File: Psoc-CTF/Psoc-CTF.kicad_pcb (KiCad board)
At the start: 2 copper layers, 68.6 x 53.3 mm, 62 parts, among them IC1 CY8C4248LQI-BL583, J3 PROG, P1 Power, P2 Analog, P3 Digital, P4 Digital, P5 CONN_01X01, P6 CONN_01X01, P7 CONN_01X01, P8 CONN_01X01, U1 AMS1117-3.3, U2 AMS1117-5.0, U3 ESP32-WROOM-32D, U4 23LC1024-E_SN, U5 SST25VF512-20-4C-SAE

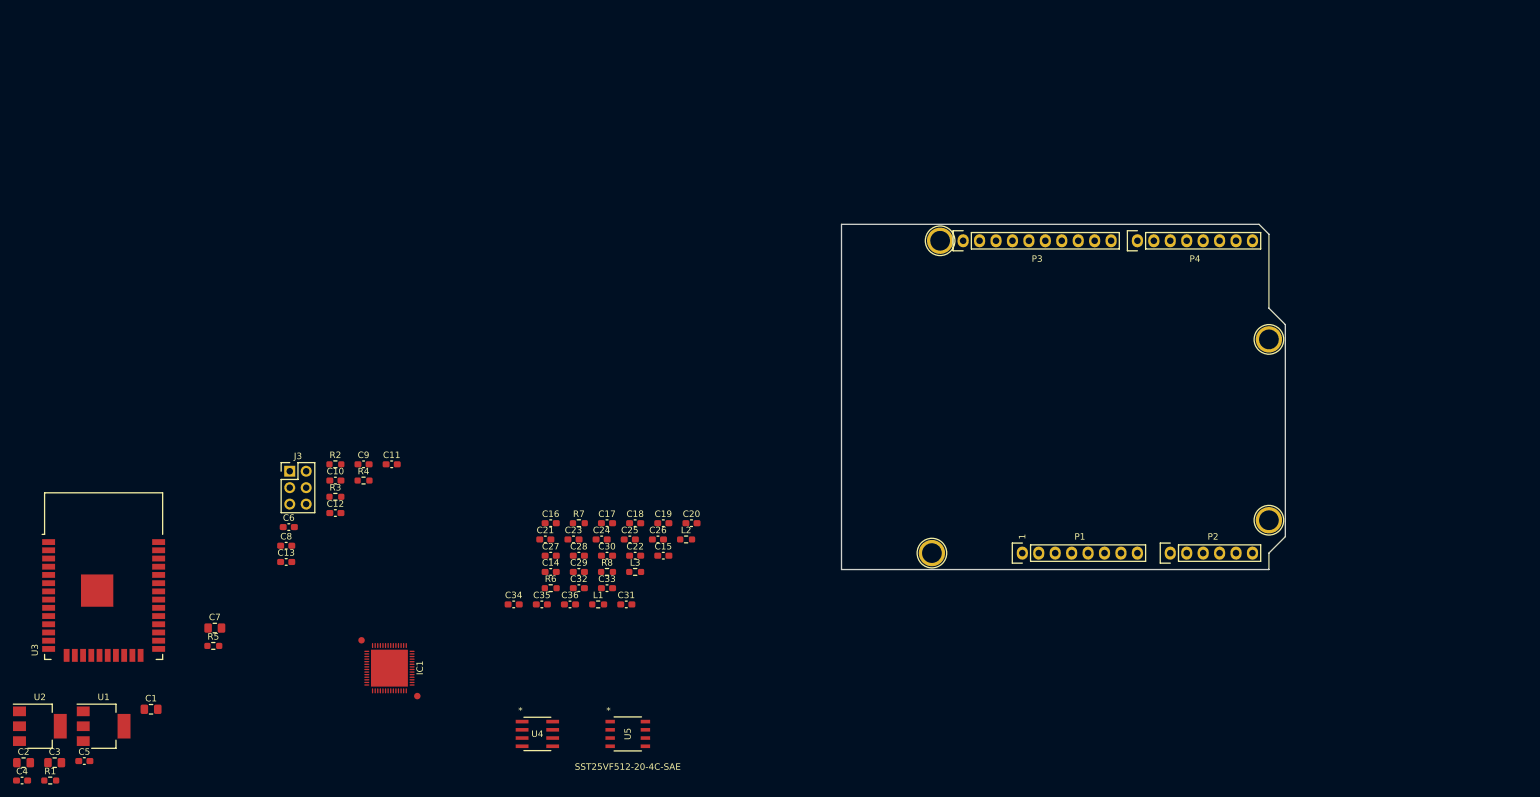
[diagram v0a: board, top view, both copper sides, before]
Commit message: Se retira las memorias flash y Ram por spi y se coloca una F-RAM por i2c
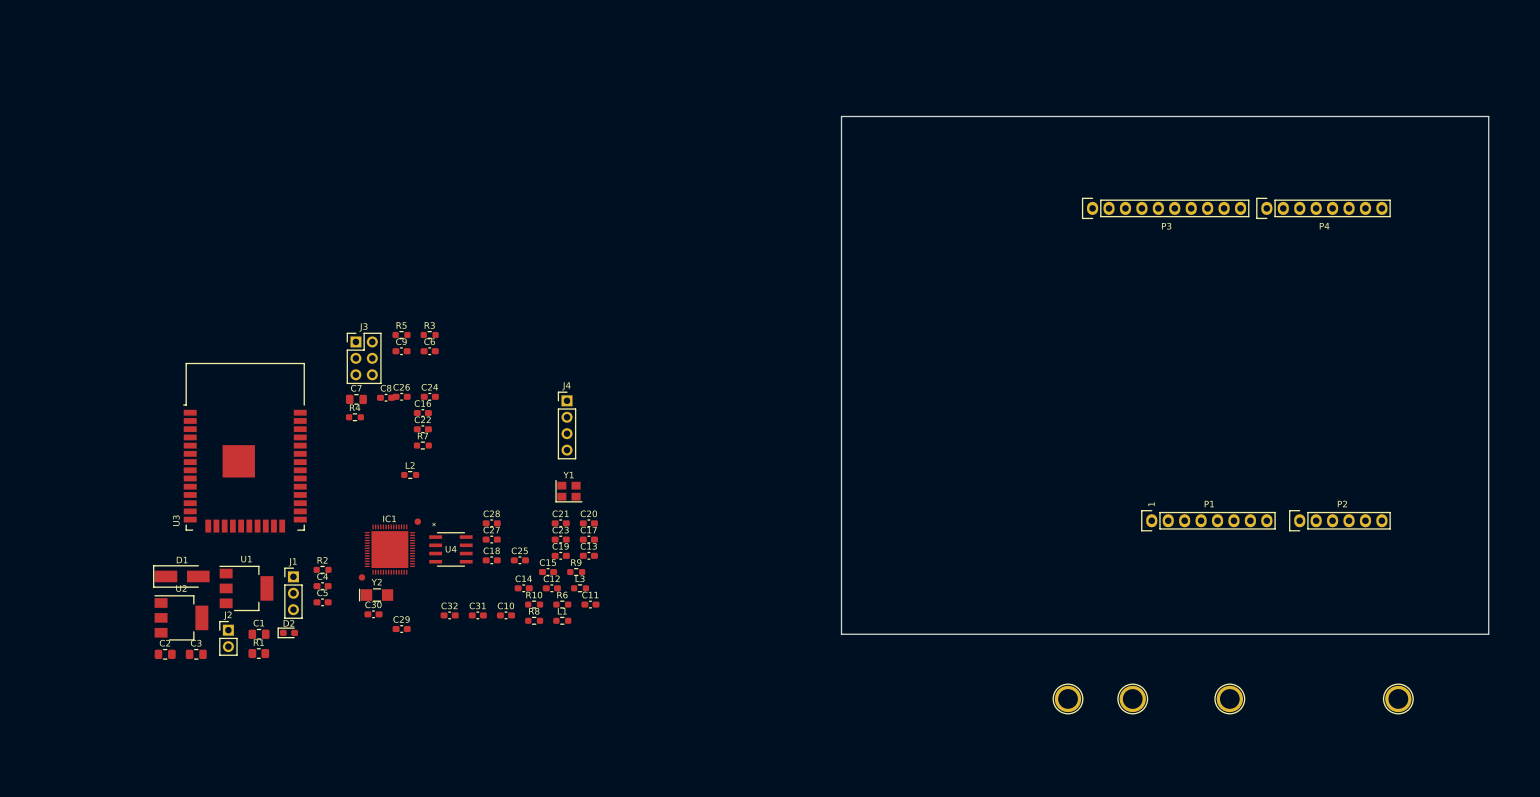
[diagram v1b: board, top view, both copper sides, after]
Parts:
- removed C33, C34: 1uF, Capacitor_SMD:C_0603_1608Metric_Pad1.08x0.95mm_HandSolder
- removed C35, C36: 0.1uF, Capacitor_SMD:C_0603_1608Metric_Pad1.08x0.95mm_HandSolder
- removed U5: SST25VF512-20-4C-SAE, Psoc-CTF:SST25VF512-20-4C-SAE
- added D1: EGF1D, Diode_SMD:D_SMA_Handsoldering, F.Cu at (9.12, 127.4)
- added D2: LED, LED_SMD:LED_0603_1608Metric_Pad1.05x0.95mm_HandSolder, F.Cu at (25.6, 136.2)
- added J1: Conn_01x03, Connector_PinHeader_2.54mm:PinHeader_1x03_P2.54mm_Vertical, F.Cu at (26.3, 127.5)
- added J2: Conn_01x02, Connector_PinHeader_2.54mm:PinHeader_1x02_P2.54mm_Vertical, F.Cu at (16.3, 135.7)
- added J4: Conn_01x04, Connector_PinHeader_2.54mm:PinHeader_1x04_P2.54mm_Vertical, F.Cu at (68.6, 100.3)
- added R10: 0, Resistor_SMD:R_0603_1608Metric_Pad0.98x0.95mm_HandSolder, F.Cu at (63.5, 131.8)
- added R9: 0, Resistor_SMD:R_0603_1608Metric_Pad0.98x0.95mm_HandSolder, F.Cu at (70.0, 126.8)
- added Y1: 24MHz, Crystal:Crystal_SMD_3225-4Pin_3.2x2.5mm, F.Cu at (68.9, 114.3)
- added Y2: 32.768Khz, Crystal:Crystal_SMD_EuroQuartz_EQ161-2Pin_3.2x1.5mm_HandSoldering, F.Cu at (39.2, 130.3)
- C10: value 1uF -> 36pF
- C11: value 1uF -> 18pF
- C13, C16, C22: value 0.1uF -> 1uF
- C14: value 36pF -> 1uF
- C15: value 18pF -> 2200pF
- C17, C18, C23, C24: value 1uF -> 0.1uF
- C19: value 2200pF -> 1uF
- C21: value 0.1uF -> 10000pF
- C25: value 10000pF -> 1uF
- R1: value 1K -> 0; footprint Resistor_SMD:R_0603_1608Metric_Pad0.98x0.95mm_HandSolder -> Resistor_SMD:R_0805_2012Metric_Pad1.20x1.40mm_HandSolder
- R2: value 10K -> 1K
- R3, R7: value 0 -> 10K
- U4: value 23LC1024-E_SN -> FM24C04B-GTR
- moved P7 76.8 mm to (156.0, 146.4)
- moved R5 56.2 mm to (43.0, 90.1)
- moved P8 55.9 mm to (171.0, 146.4)
- moved C4 55.3 mm to (30.8, 128.9)
- moved C13 46.8 mm to (72.0, 124.2)
- moved C26 45.3 mm to (43.0, 99.7)
- moved C5 44.2 mm to (30.8, 131.4)
- moved L2 43.8 mm to (44.4, 111.8)
- moved C7 41.6 mm to (36.0, 100.1)
- moved C22 38.2 mm to (46.3, 104.7)
- moved R1 37.7 mm to (21.0, 139.3)
- moved C11 37.6 mm to (72.2, 131.8)
- moved C30 37.2 mm to (38.7, 133.3)
- moved C12 35.4 mm to (66.2, 129.3)
- moved C6 34.8 mm to (47.4, 92.6)
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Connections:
- net Net-(IC1-Pad19) renamed /MCU_Target/11(**/MOSI)
- net Net-(IC1-Pad20) renamed /MCU_Target/12(MISO)
- net Net-(IC1-Pad21) renamed /MCU_Target/10(**/SS)
- net Net-(IC1-Pad22) renamed /MCU_Target/13(SCK)
- net Net-(IC1-Pad24) renamed /MCU_Target/9(**)
- net Net-(IC1-Pad25) renamed /MCU_Target/8
- net Net-(IC1-Pad28) renamed /MCU_Target/7
- net Net-(IC1-Pad29) renamed /MCU_Target/6(**)
- net Net-(IC1-Pad30) renamed /MCU_Target/5(**)
- net Net-(IC1-Pad31) renamed /MCU_Target/4
- net Net-(IC1-Pad34) renamed /MCU_Target/2
- net Net-(IC1-Pad35) renamed /MCU_Target/3(**)
- net Net-(IC1-Pad47) renamed /MCU_Target/A0
- net Net-(IC1-Pad48) renamed /MCU_Target/A1
- net Net-(IC1-Pad49) renamed /MCU_Target/A2
- net Net-(IC1-Pad50) renamed /MCU_Target/A3
- C10 pad 1: VDD -> /MCU_Target/XTAL32I
- C11 pad 1: VDD -> /MCU_Target/XTAL32O
- C12 pad 1: VDD -> /MCU_Target/XRES
- C13 pad 1: VDD -> /MCU_Target/VDDD
- C14 pad 1: /MCU_Target/XTAL32I -> /MCU_Target/VDDR
- C15 pad 1: /MCU_Target/XTAL32O -> /MCU_Target/P4.0
- C16 pad 1: /MCU_Target/XRES -> /MCU_Target/VCCD
- C19 pad 1: /MCU_Target/P4.0 -> /MCU_Target/VDDD
- C20 pad 1: /MCU_Target/VCCD -> /MCU_Target/VDDR
- C21 pad 1: /MCU_Target/VDDD -> /MCU_Target/P4.1
- C22 pad 1: /MCU_Target/VDDR -> /MCU_Target/VREF
- C25 pad 1: /MCU_Target/P4.1 -> /MCU_Target/VDDA
- C26 pad 1: /MCU_Target/VREF -> /MCU_Target/VDDR
- C27 pad 1: /MCU_Target/VDDD -> /MCU_Target/VDDA
- C31 pad 1: /MCU_Target/VDDA -> /MCU_Target/VDDR
- C32 pad 1: /MCU_Target/VDDR -> /MCU_Target/VDDA
- IC1 pad 51: Net-(IC1-Pad51) -> /MCU_Target/T_MCU_SDA
- IC1 pad 52: Net-(IC1-Pad52) -> /MCU_Target/T_MCU_SCL
- R1 pad 2: Net-(D2-Pad2) -> +3V3
- R2 pad 2: /MONITOR/EN -> Net-(D2-Pad2)
- R3 pad 1: Net-(R3-Pad1) -> VDD
- R3 pad 2: GND -> /MONITOR/EN
- R4 pad 2: Net-(R4-Pad2) -> /MCU_Target/T_MCU_SDA
- R5 pad 1: VDD -> /MCU_Target/T_MCU_SCL
- R5 pad 2: Net-(R5-Pad2) -> VDD
- R7 pad 1: /MCU_Target/P4.0 -> Net-(R7-Pad1)
- R8 pad 1: /MCU_Target/VCCD -> VDD
- R8 pad 2: /MCU_Target/VDDD -> Net-(R7-Pad1)
- U3 pad 30: /MONITOR/SPI_CLK -> Net-(U3-Pad30)
- U3 pad 31: /MONITOR/SPI_MISO -> Net-(U3-Pad31)
- U3 pad 33: /MONITOR/CE_FLASH -> /MCU_Target/T_MCU_SDA
- U3 pad 36: /MONITOR/CE_RAM -> /MCU_Target/T_MCU_SCL
- U3 pad 37: /MONITOR/SPI_MOSI -> Net-(U3-Pad37)
- U4 pad 1: /MONITOR/CE_RAM -> Net-(U4-Pad1)
- U4 pad 2: /MONITOR/SPI_MISO -> GND
- U4 pad 3: Net-(U4-Pad3) -> GND
- U4 pad 5: /MONITOR/SPI_MOSI -> /MCU_Target/T_MCU_SDA
- U4 pad 6: /MONITOR/SPI_CLK -> /MCU_Target/T_MCU_SCL
- U4 pad 7: Net-(R5-Pad2) -> Net-(R7-Pad1)
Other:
- board size 68.6 x 53.3 mm -> 100 x 80 mm

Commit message: Antena agregada, pines de programación SWD
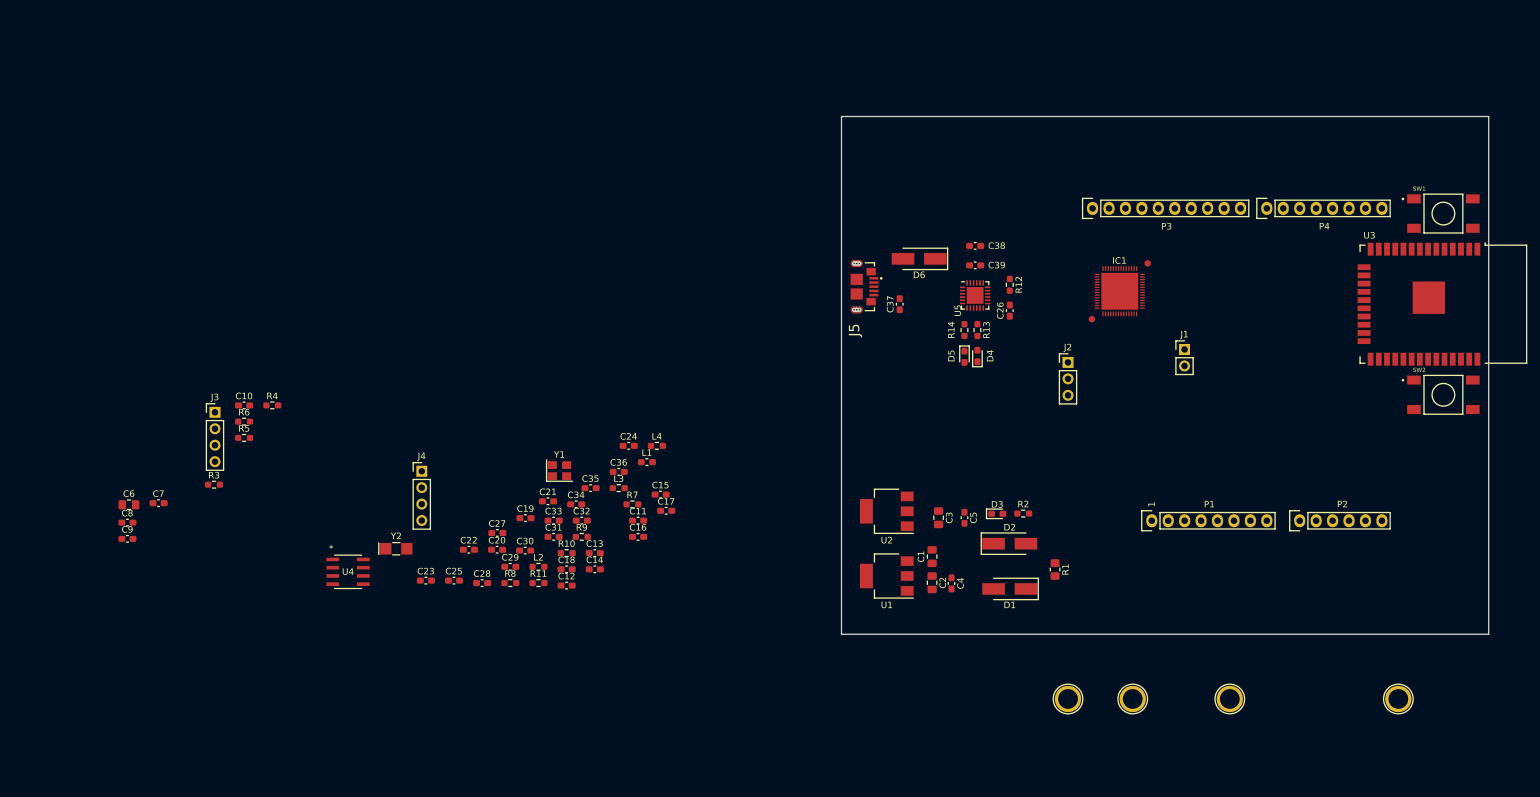
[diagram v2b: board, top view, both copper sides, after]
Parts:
- added C33: 1uF, Capacitor_SMD:C_0603_1608Metric_Pad1.08x0.95mm_HandSolder, F.Cu at (66.5, 118.8)
- added C34: 1uF, Capacitor_SMD:C_0603_1608Metric_Pad1.08x0.95mm_HandSolder, F.Cu at (70.0, 116.3)
- added C35: 0.1uF, Capacitor_SMD:C_0603_1608Metric_Pad1.08x0.95mm_HandSolder, F.Cu at (72.2, 113.8)
- added C36: 0.1uF, Capacitor_SMD:C_0603_1608Metric_Pad1.08x0.95mm_HandSolder, F.Cu at (76.6, 111.3)
- added C37: 0.1uF, Capacitor_SMD:C_0603_1608Metric_Pad1.08x0.95mm_HandSolder, F.Cu at (120.0, 85.4)
- added C38: 1uF, Capacitor_SMD:C_0603_1608Metric_Pad1.08x0.95mm_HandSolder, F.Cu at (131.6, 76.4)
- added C39: 0.1uF, Capacitor_SMD:C_0603_1608Metric_Pad1.08x0.95mm_HandSolder, F.Cu at (131.6, 79.4)
- added D3: LED, LED_SMD:LED_0603_1608Metric_Pad1.05x0.95mm_HandSolder, F.Cu at (135.1, 117.8)
- added D4: LED, LED_SMD:LED_0603_1608Metric_Pad1.05x0.95mm_HandSolder, F.Cu at (132.0, 93.4)
- added D5: LED, LED_SMD:LED_0603_1608Metric_Pad1.05x0.95mm_HandSolder, F.Cu at (130.0, 93.5)
- added D6: SSA14, Diode_SMD:D_SMA_Handsoldering, F.Cu at (123.0, 78.4)
- added J5: USB3076-XX-X_REVC, Psoc-CTF:microUSB, F.Cu at (113.3, 82.7)
- added L4: FBMH1608HM331-T, Resistor_SMD:R_0603_1608Metric_Pad0.98x0.95mm_HandSolder, F.Cu at (82.5, 107.3)
- added R11: 0, Resistor_SMD:R_0603_1608Metric_Pad0.98x0.95mm_HandSolder, F.Cu at (64.2, 128.5)
- added R12: 10k, Resistor_SMD:R_0603_1608Metric_Pad0.98x0.95mm_HandSolder, F.Cu at (137.0, 82.4)
- added R13: 1K, Resistor_SMD:R_0603_1608Metric_Pad0.98x0.95mm_HandSolder, F.Cu at (132.0, 89.4)
- added R14: 1K, Resistor_SMD:R_0603_1608Metric_Pad0.98x0.95mm_HandSolder, F.Cu at (130.0, 89.4)
- added SW1: FSM4JSMATR, Psoc-CTF:Push_button_FSM4JSMATR, F.Cu at (204.0, 71.4)
- added SW2: FSM4JSMATR, Psoc-CTF:Push_button_FSM4JSMATR, F.Cu at (204.0, 99.4)
- added U5: CY7C65211-24LTXI, Package_DFN_QFN:QFN-24-1EP_4x4mm_P0.5mm_EP2.6x2.6mm, F.Cu at (131.6, 84.0)
- C10: value 36pF -> 0.1uF
- C11: value 18pF -> 36pF
- C12: value 0.1uF -> 18pF
- C13, C19, C25, C30, C8: value 1uF -> 0.1uF
- C15: value 2200pF -> 1uF
- C16: value 1uF -> 2200pF
- C17, C23, C27, C28: value 0.1uF -> 1uF
- C21: value 10000pF -> 1uF
- C22: value 1uF -> 10000pF
- C29: value 1uF -> 1.5pF
- C32: value 0.1uF -> 1.2pF
- C6: value 0.1uF -> 10uF; footprint Capacitor_SMD:C_0603_1608Metric_Pad1.08x0.95mm_HandSolder -> Capacitor_SMD:C_0805_2012Metric_Pad1.18x1.45mm_HandSolder
- C7: value 10uF -> 1uF; footprint Capacitor_SMD:C_0805_2012Metric_Pad1.18x1.45mm_HandSolder -> Capacitor_SMD:C_0603_1608Metric_Pad1.08x0.95mm_HandSolder
- D1: value EGF1D -> SSA14
- D2: value LED -> SSA14; footprint LED_SMD:LED_0603_1608Metric_Pad1.05x0.95mm_HandSolder -> Diode_SMD:D_SMA_Handsoldering
- J1: value Conn_01x03 -> Conn_01x02; footprint Connector_PinHeader_2.54mm:PinHeader_1x03_P2.54mm_Vertical -> Connector_PinHeader_2.54mm:PinHeader_1x02_P2.54mm_Vertical
- J2: value Conn_01x02 -> Conn_01x03; footprint Connector_PinHeader_2.54mm:PinHeader_1x02_P2.54mm_Vertical -> Connector_PinHeader_2.54mm:PinHeader_1x03_P2.54mm_Vertical
- J3: value PROG -> Prog; footprint Connector_PinHeader_2.54mm:PinHeader_2x03_P2.54mm_Vertical -> Connector_PinHeader_2.54mm:PinHeader_1x04_P2.54mm_Vertical
- L1: value FBMH1608HM331-T -> 6.8nH; footprint Resistor_SMD:R_0603_1608Metric_Pad0.98x0.95mm_HandSolder -> Inductor_SMD:L_0603_1608Metric_Pad1.05x0.95mm_HandSolder
- R8: value 0 -> 10K
- U1: value AMS1117-3.3 -> AMS1117-5.0
- U2: value AMS1117-5.0 -> AMS1117-3.3
- moved U3 183.8 mm to (201.0, 85.4), turned to 270 degrees
- moved J1 142.1 mm to (164.0, 92.4)
- moved J2 136.2 mm to (146.0, 94.4)
- moved D1 127.9 mm to (137.0, 129.4), turned to 180 degrees
- moved R1 123.7 mm to (144.0, 126.4), turned to 270 degrees
- moved IC1 119.6 mm to (154.0, 83.4)
- moved C2 119.0 mm to (125.0, 128.4), turned to 270 degrees
- moved C3 116.6 mm to (126.0, 118.4), turned to 270 degrees
- moved D2 112.2 mm to (137.0, 122.4)
- moved U2 110.2 mm to (118.0, 117.4), turned to 180 degrees
- moved R2 108.6 mm to (139.1, 117.7)
- moved C1 104.7 mm to (125.0, 124.4), turned to 90 degrees
- moved C5 100.0 mm to (130.0, 118.4), turned to 270 degrees
- moved U1 98.9 mm to (118.0, 127.4), turned to 180 degrees
- moved C4 97.2 mm to (128.0, 128.5), turned to 270 degrees
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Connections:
- C10 pad 1: /MCU_Target/XTAL32I -> /MONITOR/BOOT
- C11 pad 1: /MCU_Target/XTAL32O -> /MCU_Target/XTAL32I
- C12 pad 1: /MCU_Target/XRES -> /MCU_Target/XTAL32O
- C13 pad 1: /MCU_Target/VDDD -> /MCU_Target/XRES
- C14 pad 1: /MCU_Target/VDDR -> /MCU_Target/VDDD
- C15 pad 1: /MCU_Target/P4.0 -> /MCU_Target/VDDR
- C16 pad 1: /MCU_Target/VCCD -> /MCU_Target/P4.0
- C17 pad 1: /MCU_Target/VDDD -> /MCU_Target/VCCD
- C18 pad 1: /MCU_Target/VDDR -> /MCU_Target/VDDD
- C19 pad 1: /MCU_Target/VDDD -> /MCU_Target/VDDR
- C2 pad 1: +3V3 -> /power_supply/5VExt
- C20 pad 1: /MCU_Target/VDDR -> /MCU_Target/VDDD
- C21 pad 1: /MCU_Target/P4.1 -> /MCU_Target/VDDR
- C22 pad 1: /MCU_Target/VREF -> /MCU_Target/P4.1
- C23 pad 1: /MCU_Target/VDDD -> /MCU_Target/VREF
- C24 pad 1: /MCU_Target/VDDR -> /MCU_Target/VDDD
- C25 pad 1: /MCU_Target/VDDA -> /MCU_Target/VDDR
- C26 pad 1: /MCU_Target/VDDR -> Net-(C26-Pad1)
- C29 pad 1: /MCU_Target/VDDA -> GND
- C29 pad 2: GND -> /MCU_Target/ANT
- C3 pad 1: /power_supply/5VExt -> +3V3
- C30 pad 1: /MCU_Target/VDDR -> /MCU_Target/VDDA
- C32 pad 1: /MCU_Target/VDDA -> GND
- C4 pad 1: +3V3 -> /power_supply/5VExt
- C5 pad 1: /power_supply/5VExt -> +3V3
- C6 pad 1: /MONITOR/EN -> VDD
- C9 pad 1: VDD -> /MONITOR/EN
- D1 pad 2: VDD -> /MCU_Target/3V3SWD
- D2 pad 1: GND -> VDD
- D2 pad 2: Net-(D2-Pad2) -> +3V3
- IC1 pad 12: Net-(IC1-Pad12) -> /MCU_Target/ANT
- IC1 pad 26: Net-(IC1-Pad26) -> /MCU_Target/SWDIO
- IC1 pad 27: Net-(IC1-Pad27) -> /MCU_Target/SWCLK
- J1 pad 1: /MCU_Target/5VSERIAL -> GND
- J1 pad 2: +5V -> /MCU_Target/AMP_READ
- J2 pad 1: GND -> /MCU_Target/5VBUS
- J2 pad 2: /MCU_Target/AMP_READ -> +5V
- J3 pad 1: /MONITOR/U0-TX -> GND
- J3 pad 2: /MONITOR/U0-RX -> /MONITOR/U0-TX
- J3 pad 3: /MONITOR/EN -> /MONITOR/U0-RX
- J3 pad 4: GND -> Net-(J3-Pad4)
- J4 pad 1: /MCU_Target/5VSERIAL -> /MCU_Target/3V3SWD
- J4 pad 2: GND -> /MCU_Target/SWDIO
- J4 pad 3: /MCU_Target/1(Tx) -> /MCU_Target/SWCLK
- J4 pad 4: /MCU_Target/0(Rx) -> GND
- L1 pad 1: VDD -> GND
- L1 pad 2: /MCU_Target/VDDR -> /MCU_Target/ANT
- L2 pad 2: /MCU_Target/VDDA -> /MCU_Target/VDDR
- L3 pad 2: /MCU_Target/VDDD -> /MCU_Target/VDDA
- R10 pad 1: /MCU_Target/VCCD -> /MCU_Target/P4.0
- R10 pad 2: /MCU_Target/VDDD -> GND
- R2 pad 2: Net-(D2-Pad2) -> Net-(D3-Pad2)
- R3 pad 2: /MONITOR/EN -> /MCU_Target/T_MCU_SDA
- R4 pad 1: VDD -> /MCU_Target/T_MCU_SCL
- R4 pad 2: /MCU_Target/T_MCU_SDA -> VDD
- R5 pad 1: /MCU_Target/T_MCU_SCL -> VDD
- R5 pad 2: VDD -> /MONITOR/EN
- R6 pad 1: /MCU_Target/VDDD -> VDD
- R6 pad 2: /MCU_Target/XRES -> /MONITOR/BOOT
- R7 pad 1: Net-(R7-Pad1) -> /MCU_Target/VDDD
- R7 pad 2: GND -> /MCU_Target/XRES
- R8 pad 1: VDD -> Net-(R8-Pad1)
- R8 pad 2: Net-(R7-Pad1) -> GND
- R9 pad 1: /MCU_Target/P4.0 -> VDD
- R9 pad 2: GND -> Net-(R8-Pad1)
- U1 pad 2: +3V3 -> /power_supply/5VExt
- U1 pad 3: +5V -> +12V
- U2 pad 2: /power_supply/5VExt -> +3V3
- U2 pad 3: +12V -> +5V
- U4 pad 7: Net-(R7-Pad1) -> Net-(R8-Pad1)
